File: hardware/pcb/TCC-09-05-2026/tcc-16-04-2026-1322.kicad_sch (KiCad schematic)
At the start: 79 parts, among them J2 Conn_02x20_Odd_Even, J3 Conn_01x10_Pin, J4 Conn_01x10_Pin, SW1 SW_Push, SW10 SW_Push, SW11 SW_Push, SW12 SW_Push, SW13 SW_Push, SW14 SW_Push, SW15 SW_Push, SW16 SW_Push, SW17 SW_Push, SW18 SW_Push, SW19 SW_Push, SW2 SW_Push, SW20 SW_Push, SW21 SW_Push, SW22 SW_Push, SW23 SW_Push, SW24 SW_Push, SW25 SW_Push, SW26 SW_Push, SW27 SW_Push, SW28 SW_Push, SW29 SW_Push, SW3 SW_Push, SW30 SW_Push, SW31 SW_Push, SW32 SW_Push, SW33 SW_Push, SW34 SW_Push, SW35 SW_Push, SW36 SW_Push, SW37 SW_Push, SW38 SW_Push, SW4 SW_Push, SW5 SW_Push, SW6 SW_Push, SW7 SW_Push, SW8 SW_Push, SW9 SW_Push

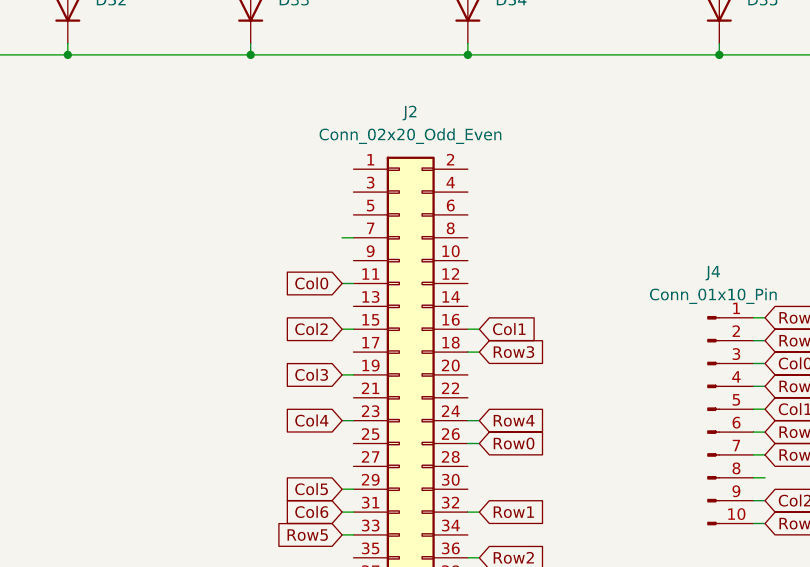
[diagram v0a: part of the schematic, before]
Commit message: feature/alteracoes-furos-footprint
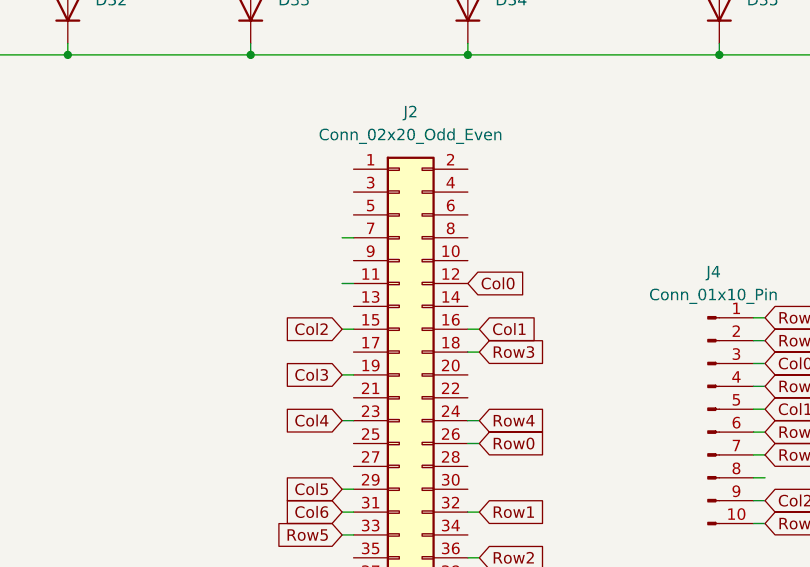
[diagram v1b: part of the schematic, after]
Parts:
- J3, J4: footprint Connector_PinHeader_2.00mm:PinHeader_2x05_P2.00mm_Vertical -> Connector_PinHeader_2.54mm:PinHeader_2x05_P2.54mm_Vertical
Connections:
- net Col0: now also J2.12 (Pin_12); no longer J2.11 (Pin_11)
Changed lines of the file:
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@@
 		)
 	)
+	(global_label "Col0"
+		(shape input)
+		(at 78.74 143.51 0)
+		(fields_autoplaced yes)
+		(effects
+			(font
+				(size 1.27 1.27)
+			)
+			(justify left)
+		)
+		(property "Intersheetrefs" "${INTERSHEET_REFS}"
+			(at 86.0189 143.51 0)
+			(hide yes)
+			(show_name no)
+			(do_not_autoplace no)
+			(effects
+				(font
+					(size 1.27 1.27)
+				)
+				(justify left)
+			)
+		)
+	)
 	(global_label "Row0"
 		(shape input)
@@
 		)
 	)
-	(global_label "Col0"
-		(shape input)
-		(at 64.77 143.51 180)
-		(fields_autoplaced yes)
-		(effects
-			(font
-				(size 1.27 1.27)
-			)
-			(justify right)
-		)
-		(property "Intersheetrefs" "${INTERSHEET_REFS}"
-			(at 57.4911 143.51 0)
-			(hide yes)
-			(show_name no)
-			(do_not_autoplace no)
-			(effects
-				(font
-					(size 1.27 1.27)
-				)
-				(justify right)
-			)
-		)
-	)
 	(global_label "Col4"
 		(shape input)
@@
 			)
 		)
-		(property "Footprint" "Connector_PinHeader_2.00mm:PinHeader_2x05_P2.00mm_Vertical"
+		(property "Footprint" "Connector_PinHeader_2.54mm:PinHeader_2x05_P2.54mm_Vertical"
 			(at 105.41 157.48 0)
 			(hide yes)
@@
 			)
 		)
-		(property "Footprint" "Connector_PinHeader_2.00mm:PinHeader_2x05_P2.00mm_Vertical"
+		(property "Footprint" "Connector_PinHeader_2.54mm:PinHeader_2x05_P2.54mm_Vertical"
 			(at 135.89 156.21 0)
 			(hide yes)
